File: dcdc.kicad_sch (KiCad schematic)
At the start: 58 parts, among them J301 Conn_01x01, J302 Conn_01x01, J303 Conn_01x01, J304 Conn_01x01, J305 Conn_01x01, Q301 MMBT3904, T301 Transformer_SP_1S, U301 L78L33_SOT89, U302 LT3439, U303 24AA02-OT, U304 TMP117, U305 LT3045xMSE

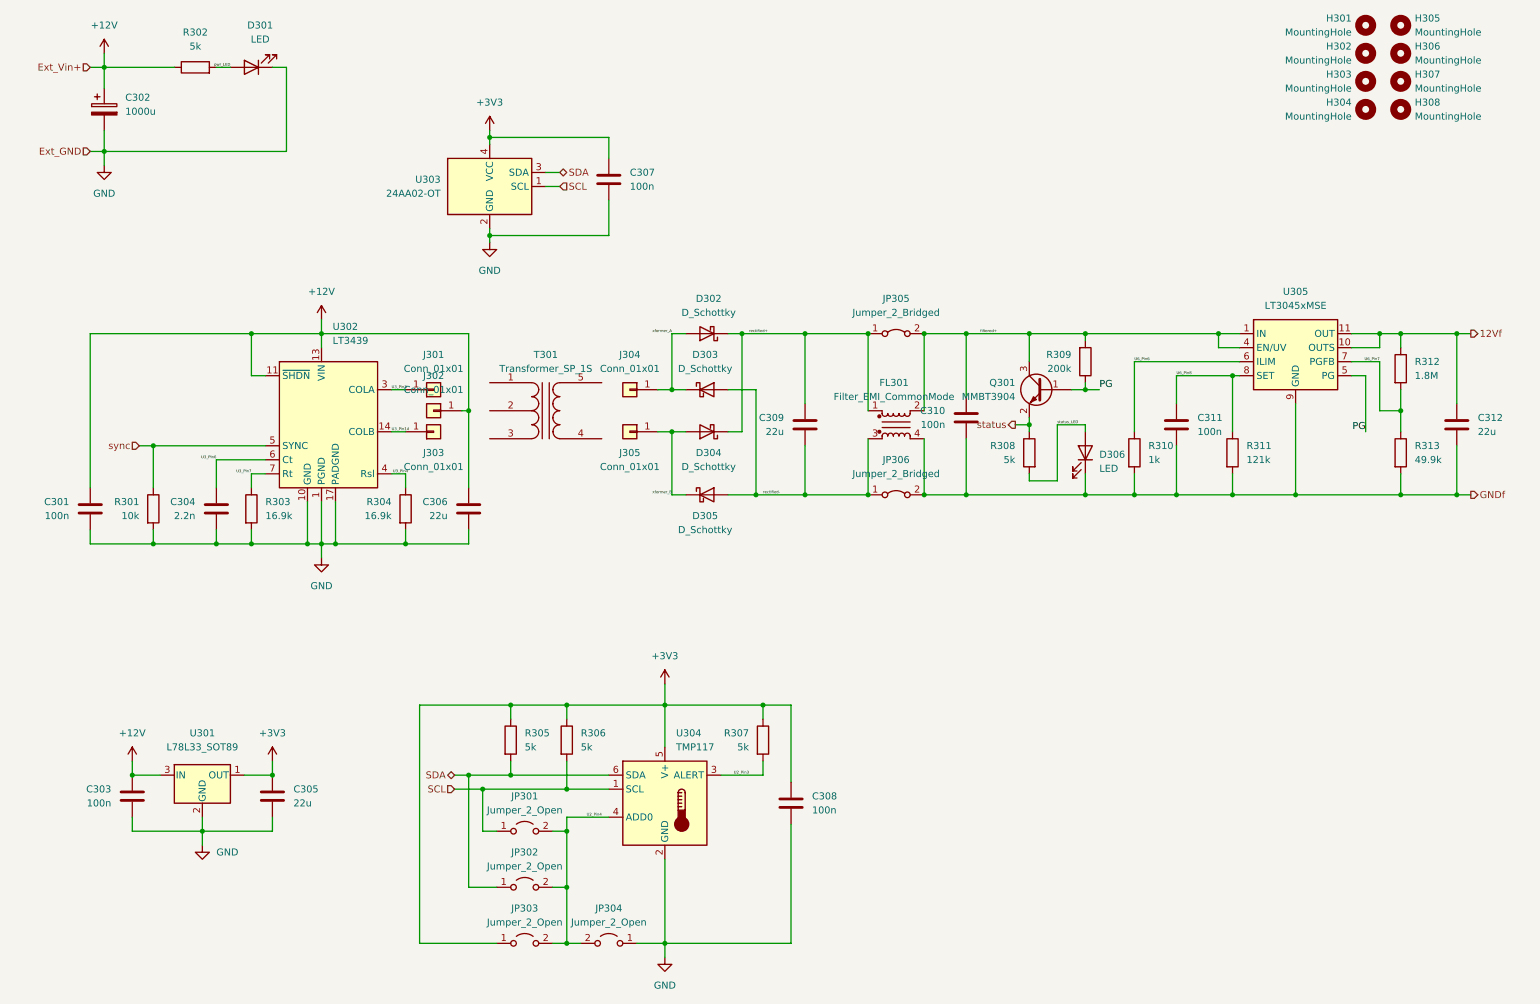
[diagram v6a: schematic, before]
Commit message: schematics updated to rev.2
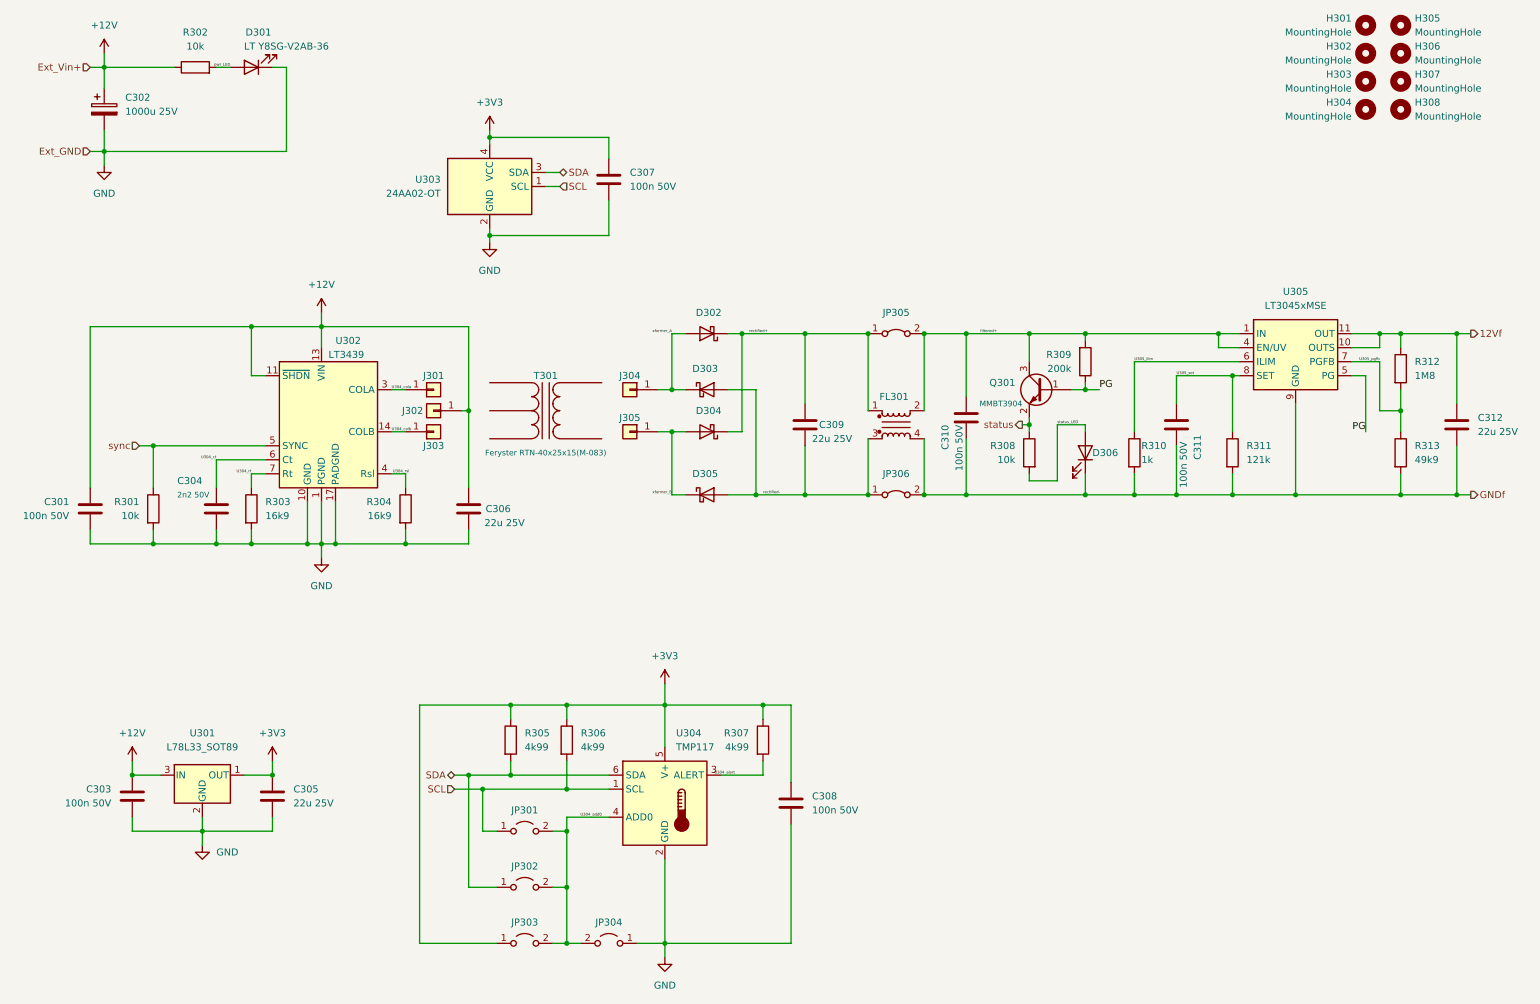
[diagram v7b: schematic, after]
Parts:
- C301, C303, C307, C308, C310, C311: value 100n -> 100n 50V
- C302: value 1000u -> 1000u 25V
- C304: value 2.2n -> 2n2 50V
- C305, C306, C309, C312: value 22u -> 22u 25V
- D301, D306: value LED -> LT Y8SG-V2AB-36
- D302, D303, D304, D305: value D_Schottky -> PMEG6010CEH
- FL301: value Filter_EMI_CommonMode -> B82793C0206N265
- H301, H302, H303, H304, H305, H306, H307, H308, J301, J302, J303, J304, J305, JP301, JP302, JP303, JP304, JP305, JP306: now left out of the parts list
- R302, R308: value 5k -> 10k
- R303, R304: value 16.9k -> 16k9
- R305, R306, R307: value 5k -> 4k99
- R312: value 1.8M -> 1M8
- R313: value 49.9k -> 49k9
- T301: value Transformer_SP_1S -> Feryster RTN-40x25x15(M-083)
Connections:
- net U2_Pin3 renamed U304_alert
- net U2_Pin4 renamed U304_add0
- net U3_Pin14 renamed U304_colb
- net U3_Pin3 renamed U304_cola
- net U3_Pin4 renamed U304_rsl
- net U3_Pin6 renamed U304_ct
- net U3_Pin7 renamed U304_rt
- net U6_Pin6 renamed U305_ilim
- net U6_Pin7 renamed U305_pgfb
- net U6_Pin8 renamed U305_set
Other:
- company: (none) -> RPG
- title: (none) -> DC-DC converter & misc

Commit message: asdf
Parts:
- removed JP305, JP306: Jumper_2_Bridged, Jumper:SolderJumper-2_P1.3mm_Bridged_RoundedPad1.0x1.5mm, symbol Jumper:Jumper_2_Bridged
- added C313: 22u 25V, Capacitor_SMD:C_1206_3216Metric, symbol Device:C
- added JP305, JP306: Jumper_2_Open, Jumper:SolderJumper-2_P1.3mm_Open_RoundedPad1.0x1.5mm, symbol Jumper:Jumper_2_Open
- R311: value 121k -> 120k
- renumbered C309 to C308, C308 to C309
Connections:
- net 12Vf: now also C313.1
- net GNDf: now also C313.2, JP306.2 (B)
- net filtered+: now also JP305.2 (B)
- net rectified+: now also JP305.1 (A)
- net rectified-: now also JP306.1 (A)
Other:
- moved on the sheet: C308, C310, C311, C312, D302, D303, D304, D305, D306, FL301, J304, J305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
